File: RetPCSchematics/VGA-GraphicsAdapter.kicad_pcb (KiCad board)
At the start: 2 copper layers, 200.7 x 139.7 mm, 26 parts, among them X1 DGOF5S3

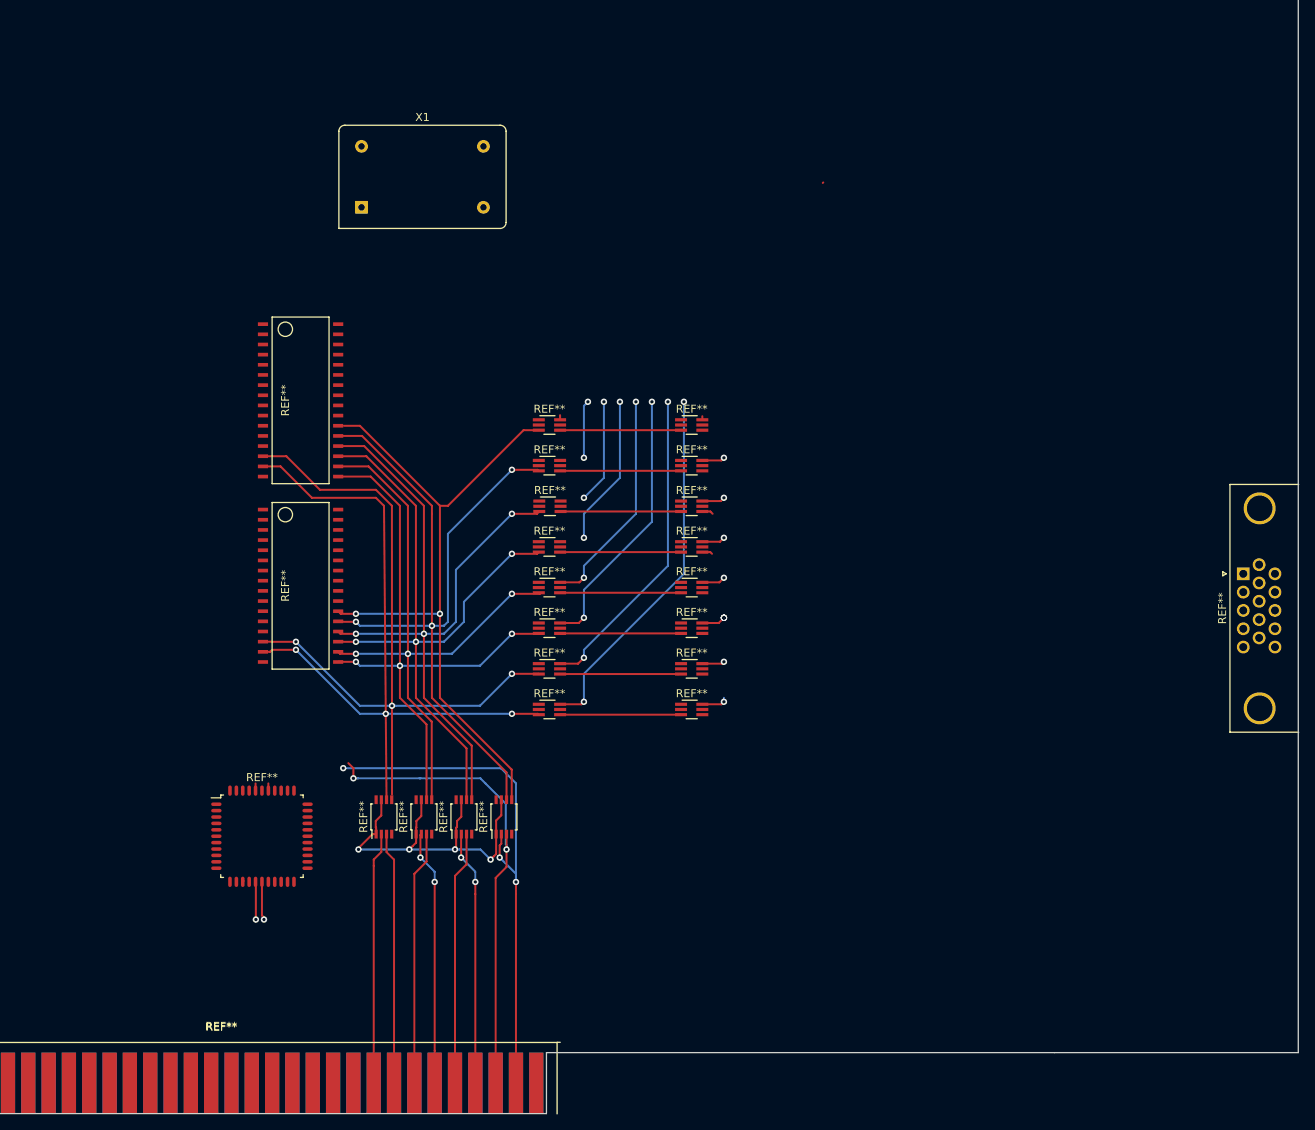
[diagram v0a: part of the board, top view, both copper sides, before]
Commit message: Made Revision 2.0.1 for the grahpics card and added external libraries
Better adress handling and data loading. Changed GPU to Atmega 640. Added external libraries for footprints and schematic symbols. Changed to DVI-D output format
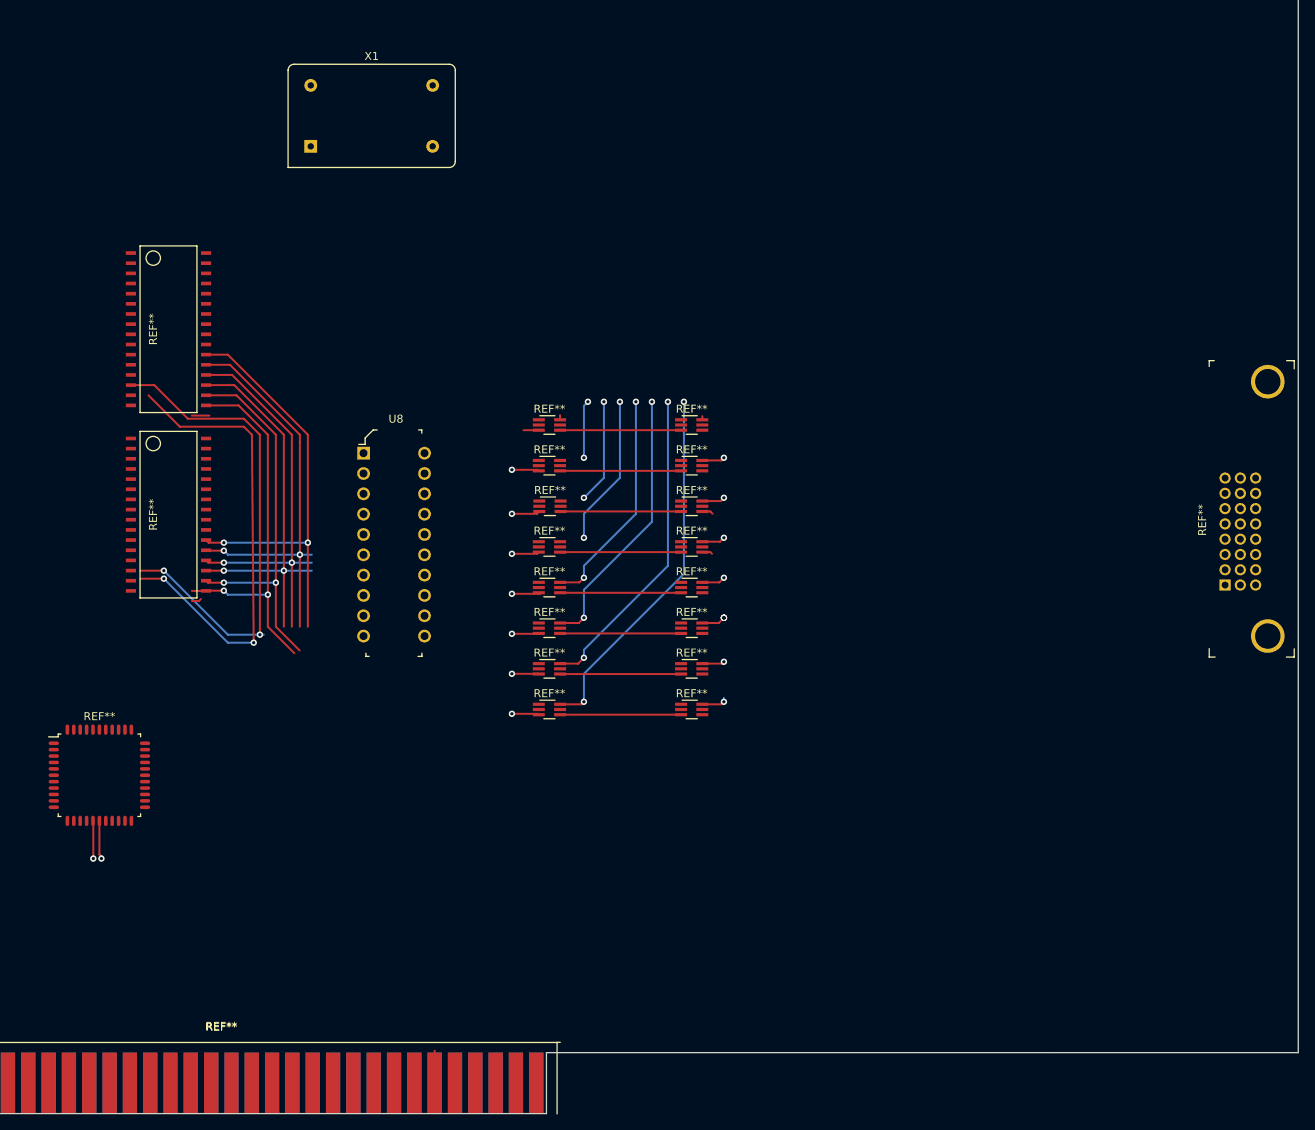
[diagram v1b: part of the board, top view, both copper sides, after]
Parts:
- removed the REF** at (136.9, 135.6)
- removed the REF** at (121.9, 135.6)
- removed the REF** at (229.3, 105.2)
- removed the REF** at (131.9, 135.6)
- removed the REF** at (126.9, 135.6)
- added REF**: DVI_Female_74320-9004, digikey-footprints:DVI_Female_74320-9004, F.Cu at (232.4, 113.0)
- added U8: SN74LVC245AN, digikey-footprints:DIP-20_W7.62mm, F.Cu at (119.4, 90.2)
- moved REF** 21.7 mm to (86.4, 130.4)
- moved REF** 18.8 mm to (95.0, 74.7)
- moved REF** 18.8 mm to (95.0, 97.9)
- moved X1 9.92 mm to (112.8, 51.8)
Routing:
- net (no net): track 1397.2 -> 796.9 mm, vias 61 -> 48

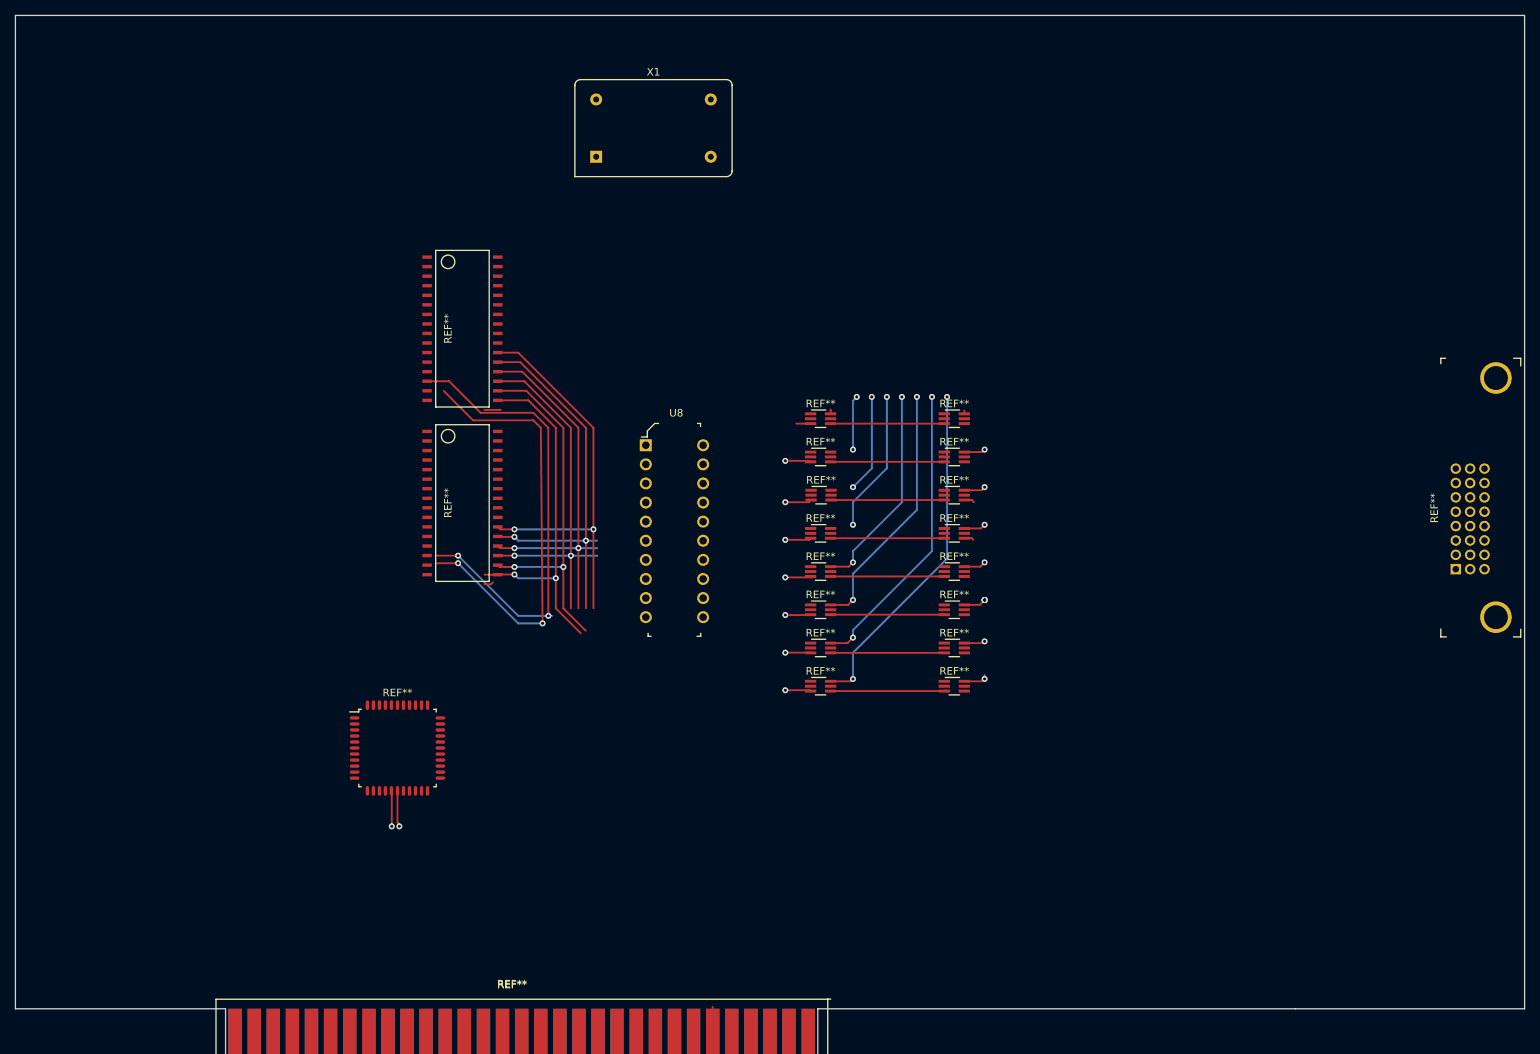
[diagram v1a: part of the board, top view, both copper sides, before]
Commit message: Added more control singals and started rerouting
Added controlsignals and started rerouting pcb to rev 2.0.1
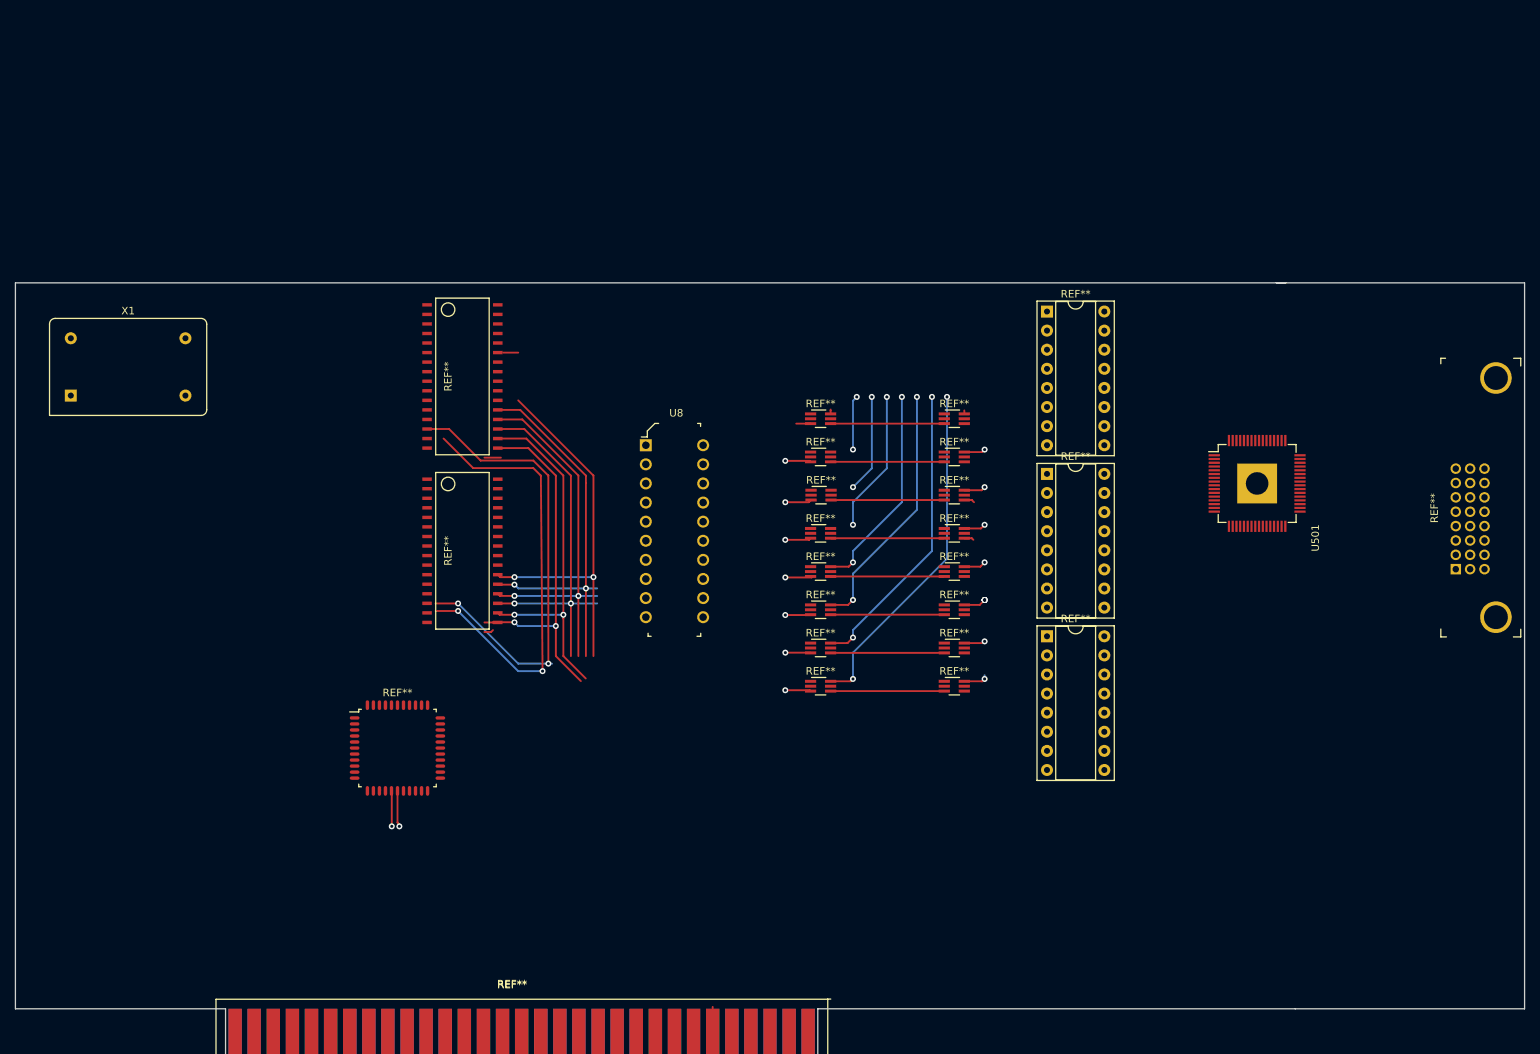
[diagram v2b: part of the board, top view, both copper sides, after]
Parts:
- added REF**: DIP-16_W7.62mm_Socket, Package_DIP:DIP-16_W7.62mm_Socket, F.Cu at (172.7, 115.6)
- added REF**: DIP-16_W7.62mm_Socket, Package_DIP:DIP-16_W7.62mm_Socket, F.Cu at (172.7, 72.4)
- added REF**: DIP-16_W7.62mm_Socket, Package_DIP:DIP-16_W7.62mm_Socket, F.Cu at (172.7, 94.0)
- added U501: TFP410, retsmd:HQFP-64_10x10mm_Pitch0.5mm_handsoldering, F.Cu at (200.7, 95.2)
- moved X1 76.7 mm to (42.9, 83.6)
- moved REF** 6.35 mm to (95.0, 104.2)
- moved REF** 6.35 mm to (95.0, 81.0)
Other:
- board size 200.7 x 139.7 mm -> 200.7 x 104.1 mm

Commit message: sync
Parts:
- removed the REF** at (172.7, 115.6)
- removed the REF** at (160.4, 107.0)
- removed the REF** at (160.4, 101.9)
- removed the REF** at (160.4, 96.8)
- removed the REF** at (160.4, 91.7)
- removed the REF** at (160.4, 86.6)
- removed the REF** at (142.6, 112.0)
- removed the REF** at (142.6, 107.0)
- removed the REF** at (142.6, 101.9)
- removed the REF** at (142.7, 96.8)
- removed the REF** at (142.6, 91.7)
- removed the REF** at (172.7, 72.4)
- removed the REF** at (172.7, 94.0)
- removed the REF** at (160.4, 122.2)
- removed the REF** at (160.4, 117.1)
- removed the REF** at (142.6, 122.2)
- removed the REF** at (142.6, 117.1)
- removed the REF** at (160.4, 112.0)
- added REF**: SOT-363_SC-70-6_Handsoldering, Package_TO_SOT_SMD:SOT-363_SC-70-6_Handsoldering, F.Cu at (185.7, 102.0)
- added REF**: SOT-363_SC-70-6_Handsoldering, Package_TO_SOT_SMD:SOT-363_SC-70-6_Handsoldering, F.Cu at (185.7, 96.9)
- added REF**: SOT-363_SC-70-6_Handsoldering, Package_TO_SOT_SMD:SOT-363_SC-70-6_Handsoldering, F.Cu at (185.7, 91.9)
- added REF**: SOT-363_SC-70-6_Handsoldering, Package_TO_SOT_SMD:SOT-363_SC-70-6_Handsoldering, F.Cu at (185.7, 86.8)
- added REF**: SOT-363_SC-70-6_Handsoldering, Package_TO_SOT_SMD:SOT-363_SC-70-6_Handsoldering, F.Cu at (185.7, 81.7)
- added REF**: SOT-363_SC-70-6_Handsoldering, Package_TO_SOT_SMD:SOT-363_SC-70-6_Handsoldering, F.Cu at (185.7, 76.6)
- added REF**: SOT-363_SC-70-6_Handsoldering, Package_TO_SOT_SMD:SOT-363_SC-70-6_Handsoldering, F.Cu at (185.7, 71.5)
- moved REF** 96.7 mm to (182.2, 117.9)
- moved REF** 86.8 mm to (184.4, 135.4)
- moved REF** 47.6 mm to (185.7, 66.5)
- moved U8 47.6 mm to (162.4, 70.0)
- moved REF** 43.7 mm to (136.5, 67.4)
- moved REF** 43.7 mm to (136.5, 90.6)
- moved X1 42.9 mm to (85.3, 77.5)
- moved REF** 29.9 mm to (244.5, 85.7)
- moved U501 24.0 mm to (215.6, 76.5)
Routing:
- net (no net): track 796.9 -> 473.6 mm, vias 48 -> 25
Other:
- board size 200.7 x 104.1 mm -> 183.4 x 101.3 mm

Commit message: Finalised schematic and started routing
Final schematic, assigned footprints and started routing
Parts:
- removed REF**: DVI_Female_74320-9004, digikey-footprints:DVI_Female_74320-9004
- removed REF**: QFP-44_10x10_Pitch0.8mm, RetPC:QFP-44_10x10_Pitch0.8mm
- removed REF** (x2): SOJ-32, SMD_Packages:SOJ-32
- removed REF** (x8): SOT-363_SC-70-6_Handsoldering, Package_TO_SOT_SMD:SOT-363_SC-70-6_Handsoldering
- removed REF**: 8Bit_ISA_BUS, RetPC:8Bit_ISA_BUS
- removed U501: TFP410, retsmd:HQFP-64_10x10mm_Pitch0.5mm_handsoldering
- added J1: Bus_ISA_8bit, RetPC:8Bit_ISA_BUS, F.Cu at (184.2, 134.6)
- added J2: 74320-9004, digikey-footprints:DVI_Female_74320-9004, F.Cu at (243.8, 99.1)
- added R1: 4.7k, Resistor_THT:R_Axial_DIN0411_L9.9mm_D3.6mm_P5.08mm_Vertical, F.Cu at (342.9, 96.5)
- added R2: 4.7k, Resistor_THT:R_Axial_DIN0411_L9.9mm_D3.6mm_P7.62mm_Vertical, F.Cu at (341.2, 83.2)
- added R3: 4.7k, Resistor_THT:R_Axial_DIN0411_L9.9mm_D3.6mm_P7.62mm_Vertical, F.Cu at (341.2, 87.4)
- added R4: 4.7k, Resistor_THT:R_Axial_DIN0411_L9.9mm_D3.6mm_P7.62mm_Vertical, F.Cu at (341.2, 91.5)
- added R5: 4.7k, Resistor_THT:R_Axial_DIN0411_L9.9mm_D3.6mm_P7.62mm_Vertical, F.Cu at (341.3, 184.4)
- added R6: 4.7k, Resistor_THT:R_Axial_DIN0411_L9.9mm_D3.6mm_P7.62mm_Vertical, F.Cu at (341.6, 64.8)
- added R7: 4.7k, Resistor_THT:R_Axial_DIN0411_L9.9mm_D3.6mm_P7.62mm_Vertical, F.Cu at (340.4, 73.7)
- added U1: 74AUC2G125, Package_SO:VSSOP-8_2.3x2mm_P0.5mm, F.Cu at (204.9, 79.6)
- added U10: ATmega644P-20PU, Package_DIP:DIP-40_W15.24mm, F.Cu at (127.0, 130.8)
- added U11: 628128, Package_DIP:DIP-24_W7.62mm_Socket, F.Cu at (24.1, 99.1)
- added U12: 628128, Package_DIP:DIP-24_W7.62mm_Socket, F.Cu at (86.4, 87.6)
- added U13: SN74LVC245AN, digikey-footprints:DIP-20_W7.62mm, F.Cu at (87.6, 154.9)
- added U14: 74LS245, Package_DIP:DIP-20_W7.62mm_Socket, F.Cu at (208.3, 121.9)
- added U15: 74LVC2G240, Package_SO:VSSOP-8_2.3x2mm_P0.5mm, F.Cu at (200.0, 83.3)
- added U16: 74LVC2G240, Package_SO:VSSOP-8_2.3x2mm_P0.5mm, F.Cu at (204.9, 82.2)
- added U17: 74LVC1G18, Package_TO_SOT_SMD:SOT-23-6_Handsoldering, F.Cu at (200.2, 80.2)
- added U18: 74LVC1G18, Package_TO_SOT_SMD:SOT-23-6_Handsoldering, F.Cu at (195.5, 95.2)
- added U19: 74LVC1G18, Package_TO_SOT_SMD:SOT-23-6_Handsoldering, F.Cu at (380.7, 129.1)
- added U2: 74LVC2G240, Package_SO:VSSOP-8_2.3x2mm_P0.5mm, F.Cu at (380.5, 132.2)
- added U20: 74LVC1G18, Package_TO_SOT_SMD:SOT-23-6_Handsoldering, F.Cu at (375.8, 132.8)
- added U21: ATF22V10D, Package_DIP:DIP-24_W7.62mm_Socket, F.Cu at (328.2, 113.4)
- added U22: 74LS245, Package_DIP:DIP-22_W7.62mm_Socket, F.Cu at (200.7, 134.6)
- added U23: 74LVC1G373, Package_TO_SOT_SMD:SOT-23-6_Handsoldering, F.Cu at (356.9, 139.7)
- added U24: 74LVC1G373, Package_TO_SOT_SMD:SOT-23-6_Handsoldering, F.Cu at (375.8, 129.2)
- added U25: 74LVC1G373, Package_TO_SOT_SMD:SOT-23-6_Handsoldering, F.Cu at (339.8, 142.2)
- added U26: 74LVC1G373, Package_TO_SOT_SMD:SOT-23-6_Handsoldering, F.Cu at (393.5, 89.8)
- added U27: 74LVC1G373, Package_TO_SOT_SMD:SOT-23-6_Handsoldering, F.Cu at (204.4, 99.1)
- added U28: 74LVC1G373, Package_TO_SOT_SMD:SOT-23-6_Handsoldering, F.Cu at (369.2, 147.4)
- added U29: 74LVC1G373, Package_TO_SOT_SMD:SOT-23-6_Handsoldering, F.Cu at (369.2, 140.1)
- added U3: ATF22V10D, Package_DIP:DIP-24_W7.62mm_Socket, F.Cu at (143.5, 22.9)
- added U30: 74LVC1G373, Package_TO_SOT_SMD:SOT-23-6_Handsoldering, F.Cu at (369.2, 143.8)
- added U31: 74LVC1G373, Package_TO_SOT_SMD:SOT-23-6_Handsoldering, F.Cu at (393.5, 93.4)
- added U32: 74LVC1G373, Package_TO_SOT_SMD:SOT-23-6_Handsoldering, F.Cu at (206.9, 91.4)
- added U33: 74LVC1G373, Package_TO_SOT_SMD:SOT-23-6_Handsoldering, F.Cu at (393.5, 100.7)
- added U34: 74LVC1G373, Package_TO_SOT_SMD:SOT-23-6_Handsoldering, F.Cu at (393.5, 97.1)
- added U37: ATF22V10D, Package_DIP:DIP-24_W7.62mm_Socket, F.Cu at (221.0, 78.7)
- added U4: ATF22V10D, Package_DIP:DIP-24_W7.62mm_Socket, F.Cu at (102.9, 87.6)
- added U5: 74LS245, Package_DIP:DIP-20_W7.62mm_Socket, F.Cu at (340.8, 157.8)
- added U6: ATF22V10D, Package_DIP:DIP-24_W7.62mm_Socket, F.Cu at (114.3, 52.1)
- added U7: 74LS245, Package_DIP:DIP-20_W7.62mm_Socket, F.Cu at (212.1, 45.7)
- added U9: 74LS245, Package_DIP:DIP-20_W7.62mm_Socket, F.Cu at (179.1, 44.5)
- U8: value SN74LVC245AN -> 74LS245; footprint digikey-footprints:DIP-20_W7.62mm -> Package_DIP:DIP-20_W7.62mm_Socket
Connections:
- U8 pad 1: Net-(U8-Pad1) -> LoadEnable
- U8 pad 10: Net-(U8-Pad10) -> GND
- U8 pad 18: Net-(U8-Pad18) -> /A7
- U8 pad 19: Net-(U8-Pad19) -> GND
- U8 pad 20: Net-(U8-Pad20) -> +5V
- U8 pad 3: Net-(U8-Pad3) -> /A6
- U8 pad 4: Net-(U8-Pad4) -> /A5
- U8 pad 5: Net-(U8-Pad5) -> /A0
- U8 pad 6: Net-(U8-Pad6) -> /A0
- U8 pad 7: Net-(U8-Pad7) -> /A0
- U8 pad 8: Net-(U8-Pad8) -> /A0
- U8 pad 9: Net-(U8-Pad9) -> /A0
- X1 pad 14: Net-(X1-Pad14) -> +5V
- X1 pad 7: Net-(X1-Pad7) -> GND
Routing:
- net (no net): track 473.6 -> 423.5 mm, vias 25 -> 16
- net Net-(J1-Pad40): track 0.00 -> 7.62 mm
- net Net-(J1-Pad39): track 0.00 -> 7.62 mm
- net Net-(J1-Pad38): track 0.00 -> 7.62 mm
- net Net-(J1-Pad37): track 0.00 -> 7.62 mm
- net Net-(J1-Pad36): track 0.00 -> 7.62 mm
- net Net-(J1-Pad35): track 0.00 -> 7.62 mm
- net Net-(J1-Pad34): track 0.00 -> 7.62 mm
- net Net-(J1-Pad33): track 0.00 -> 7.62 mm
- net Net-(J1-Pad32): track 0.00 -> 4.06 mm
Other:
- board text removed: "PIC16"
- board text removed: "PROG_PIN"
